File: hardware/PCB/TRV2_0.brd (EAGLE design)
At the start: 46 x 70 mm, 51 parts, among them IC1 TMP112, IC2 IC2, IC4 CNY70, IC5 ATMEGA8-AU, U1 DRV8850_RGY_24, X1 FC-12M

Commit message: ready for gerbers
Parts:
- added ML, MR: TPB1,27, testpad:B1,27
- moved J4 1.00 mm to (43.0, 21.0)
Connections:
- net ML: now also ML.TP
- net MR: now also MR.TP
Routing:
- net MR: track 32.3 -> 36.2 mm
- net ML: track 39.6 -> 41.9 mm
- net SPI_SCLK: track 43.1 -> 44.1 mm
- net SPI_MOSI: track 45.2 -> 46.2 mm
- net SPI_NNS: track 46.0 -> 47.0 mm
- net RFMIRQ: track 71.0 -> 72.0 mm
- net SPI_MISO: track 47.1 -> 48.1 mm
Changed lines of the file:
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@@
 <attribute name="NAME" x="14.7193" y="59.4741" size="0.8128" layer="25" rot="R180"/>
 </element>
-<element name="R5" library="resistor" package="R0603" value="4K7" x="10.7696" y="30.48" locked="yes" smashed="yes" rot="R90">
-<attribute name="NAME" x="-3.175" y="29.2354" size="0.8128" layer="25"/>
-</element>
+<element name="R5" library="resistor" package="R0603" value="4K7" x="10.7696" y="30.48" locked="yes" smashed="yes" rot="R90"/>
 <element name="R6" library="resistor" package="R0603" value="4K7" x="12.3952" y="30.48" locked="yes" smashed="yes" rot="R90">
 <attribute name="NAME" x="12.87145" y="32.22625" size="0.8128" layer="25" rot="R90"/>
@@
 <attribute name="VALUE" x="13.696009375" y="55.8038" size="1.27" layer="27" rot="R180"/>
 </element>
-<element name="J4" library="con-lstb" package="MA08-1" value="" x="42.005" y="20.955" rot="R90">
-<attribute name="MF" value="" x="42.005" y="20.955" size="1.778" layer="27" rot="R90" display="off"/>
-<attribute name="OC_NEWARK" value="unknown" x="42.005" y="20.955" size="1.778" layer="27" rot="R90" display="off"/>
-<attribute name="OC_FARNELL" value="unknown" x="42.005" y="20.955" size="1.778" layer="27" rot="R90" display="off"/>
-<attribute name="MPN" value="" x="42.005" y="20.955" size="1.778" layer="27" rot="R90" display="off"/>
+<element name="J4" library="con-lstb" package="MA08-1" value="" x="43.005" y="20.955" rot="R90">
+<attribute name="MF" value="" x="43.005" y="20.955" size="1.778" layer="27" rot="R90" display="off"/>
+<attribute name="OC_NEWARK" value="unknown" x="43.005" y="20.955" size="1.778" layer="27" rot="R90" display="off"/>
+<attribute name="OC_FARNELL" value="unknown" x="43.005" y="20.955" size="1.778" layer="27" rot="R90" display="off"/>
+<attribute name="MPN" value="" x="43.005" y="20.955" size="1.778" layer="27" rot="R90" display="off"/>
 </element>
 <element name="U1" library="drv8850" package="RGY_24" value="DRV8850_RGY_24" x="11.43" y="46.99" smashed="yes">
 <attribute name="VENDOR" value="Texas Instruments" x="11.43" y="46.99" size="1.778" layer="27" display="off"/>
 <attribute name="MANUFACTURER_PART_NUMBER" value="drv8850_rgy_24" x="11.43" y="46.99" size="1.778" layer="27" display="off"/>
-<attribute name="NAME" x="6.0198" y="48.5775" size="0.8128" layer="25" ratio="6" rot="SR0"/>
+<attribute name="NAME" x="6.387075" y="49.645740625" size="0.8128" layer="25" ratio="6" rot="SR0"/>
 </element>
 <element name="R3" library="resistor" package="R0603" value="24K" x="10.795" y="42.545" smashed="yes" rot="R180">
@@
 <element name="U$1" library="opto-trans-siemens" package="SFH_325-3/4" value="SFH_325-3/4" x="4.1473375" y="68.196" smashed="yes"/>
 <element name="U$2" library="led" package="KINGBRIGHTSIDELED" value="KINGBRIGHTSIDELED" x="13.17625" y="69.05625" smashed="yes" rot="MR0"/>
+<element name="ML" library="testpad" package="B1,27" value="TPB1,27" x="5.15581875" y="48.597771875" smashed="yes">
+<attribute name="TP_SIGNAL_NAME" value="" x="4.52081875" y="46.692771875" size="1" layer="37"/>
+<attribute name="NAME" x="4.049359375" y="48.0007" size="0.8128" layer="25" ratio="10" rot="R90"/>
+<attribute name="VALUE" x="4.52081875" y="47.835771875" size="0.0254" layer="27"/>
+</element>
+<element name="MR" library="testpad" package="B1,27" value="TPB1,27" x="5.1351375" y="46.475203125" smashed="yes">
+<attribute name="TP_SIGNAL_NAME" value="" x="4.5001375" y="44.570203125" size="1" layer="37"/>
+<attribute name="NAME" x="3.93528125" y="45.843521875" size="0.8128" layer="25" ratio="10" rot="R90"/>
+<attribute name="VALUE" x="4.5001375" y="45.713203125" size="0.0254" layer="27"/>
+</element>
 </elements>
 <signals>
@@
 <wire x1="21.9456" y1="17.8816" x2="22.073025" y2="17.996384375" width="0.2032" layer="1"/>
 <wire x1="21.9456" y1="17.272" x2="39.8272" y2="17.272" width="0.2032" layer="1"/>
-<wire x1="39.8272" y1="17.272" x2="42.005" y2="17.145" width="0.2032" layer="1"/>
+<wire x1="39.8272" y1="17.272" x2="43.005" y2="17.145" width="0.2032" layer="1"/>
 </signal>
 <signal name="MI">
@@
 <wire x1="13.60238125" y1="14.621740625" x2="15.340503125" y2="14.621740625" width="0.254" layer="16"/>
 <wire x1="21.336" y1="22.1488" x2="39.8272" y2="22.1488" width="0.2032" layer="1"/>
-<wire x1="39.8272" y1="22.1488" x2="42.005" y2="22.225" width="0.2032" layer="1"/>
+<wire x1="39.8272" y1="22.1488" x2="43.005" y2="22.225" width="0.2032" layer="1"/>
 <wire x1="21.336" y1="22.1488" x2="21.27013125" y2="21.97453125" width="0.2032" layer="1"/>
 <wire x1="15.4432" y1="14.6304" x2="15.337246875" y2="14.61893125" width="0.2032" layer="16"/>
@@
 <wire x1="22.7584" y1="24.5872" x2="39.8272" y2="24.5872" width="0.2032" layer="1"/>
 <wire x1="22.1488" y1="23.9776" x2="22.7584" y2="24.5872" width="0.2032" layer="1"/>
-<wire x1="39.8272" y1="24.5872" x2="42.005" y2="24.765" width="0.2032" layer="1"/>
+<wire x1="39.8272" y1="24.5872" x2="43.005" y2="24.765" width="0.2032" layer="1"/>
 <wire x1="22.1488" y1="23.9776" x2="22.098934375" y2="23.970465625" width="0.2032" layer="1"/>
 </signal>
@@
 <wire x1="22.352" y1="19.7104" x2="39.8272" y2="19.7104" width="0.2032" layer="1"/>
 <wire x1="22.1488" y1="19.9136" x2="22.352" y2="19.7104" width="0.2032" layer="1"/>
-<wire x1="39.8272" y1="19.7104" x2="42.005" y2="19.685" width="0.2032" layer="1"/>
+<wire x1="39.8272" y1="19.7104" x2="43.005" y2="19.685" width="0.2032" layer="1"/>
 <wire x1="22.1488" y1="19.9136" x2="22.034925" y2="20.030415625" width="0.2032" layer="1"/>
 </signal>
@@
 <wire x1="20.5232" y1="7.112" x2="21.5392" y2="8.128" width="0.2032" layer="1"/>
 <wire x1="20.5232" y1="6.096" x2="20.5232" y2="7.112" width="0.2032" layer="1"/>
-<wire x1="39.8272" y1="14.4272" x2="42.005" y2="14.605" width="0.2032" layer="1"/>
+<wire x1="39.8272" y1="14.4272" x2="43.005" y2="14.605" width="0.2032" layer="1"/>
 <wire x1="20.5232" y1="6.096" x2="20.4216" y2="6.096" width="0.2032" layer="1"/>
 </signal>
@@
 <via x="8.255" y="46.355" extent="1-16" drill="0.6"/>
 <wire x1="8.37" y1="46.24" x2="8.255" y2="46.355" width="0.2032" layer="1"/>
+<contactref element="ML" pad="TP"/>
+<wire x1="5.15581875" y1="48.597771875" x2="6.5913" y2="48.597771875" width="0.2032" layer="1"/>
+<wire x1="6.5913" y1="48.597771875" x2="6.5913" y2="47.752" width="0.2032" layer="1"/>
 </signal>
 <signal name="MR">
@@
 <wire x1="7.3025" y1="46.355" x2="7.3025" y2="47.24" width="0.2032" layer="1"/>
 <wire x1="7.3025" y1="47.24" x2="9.7026" y2="47.24" width="0.2032" layer="1"/>
+<contactref element="MR" pad="TP"/>
+<wire x1="5.1351375" y1="46.475203125" x2="5.132171875" y2="46.475203125" width="0.4064" layer="1"/>
+<wire x1="5.132171875" y1="46.475203125" x2="5.132171875" y2="44.0461125" width="0.2032" layer="1"/>
+<wire x1="5.132171875" y1="44.0461125" x2="6.1479875" y2="43.0694875" width="0.2032" layer="1"/>
 </signal>
 </signals>

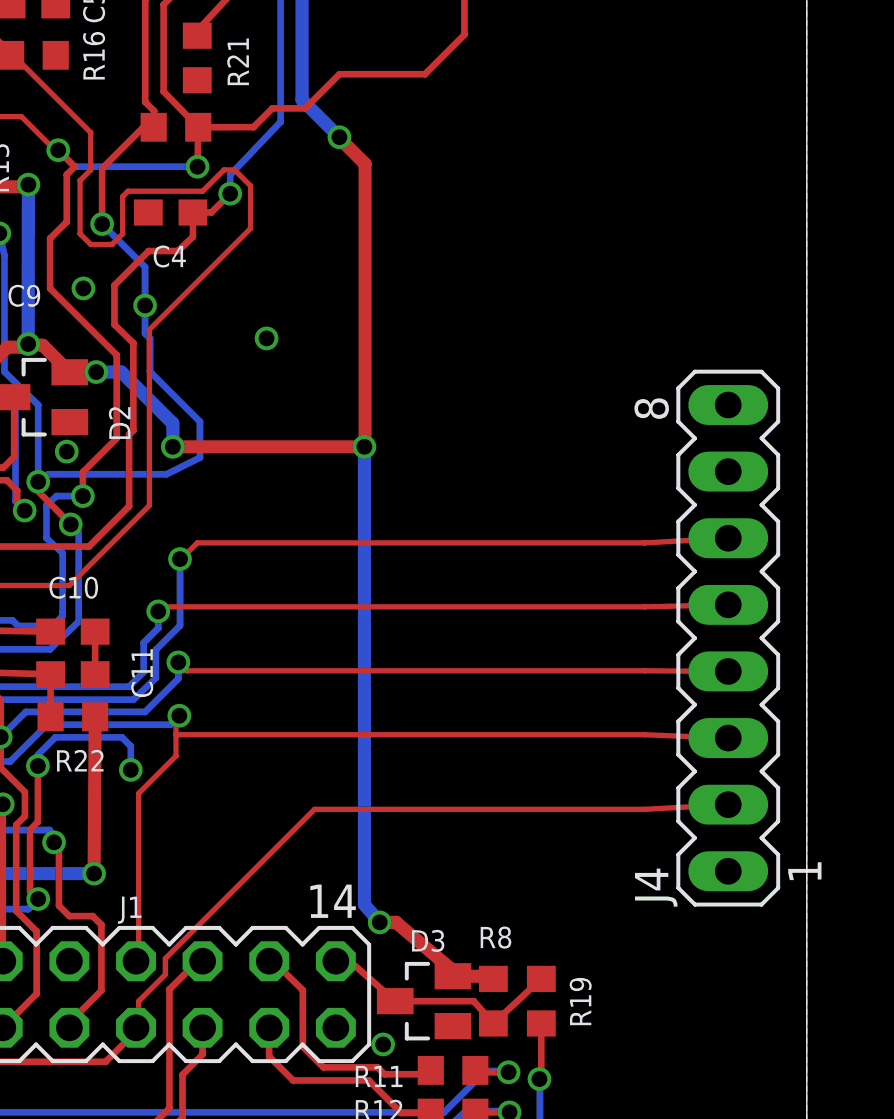
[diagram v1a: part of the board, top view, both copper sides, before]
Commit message: added power to radio module connector
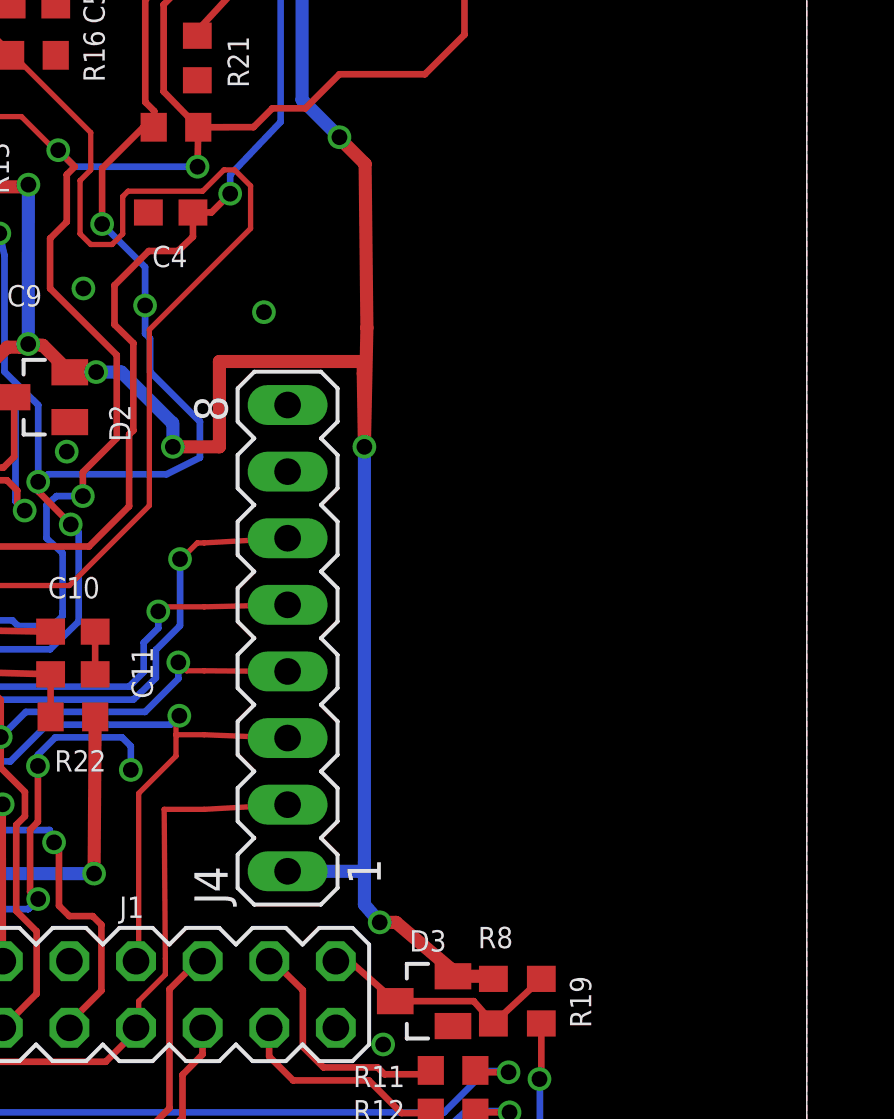
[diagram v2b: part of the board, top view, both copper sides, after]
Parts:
- moved J4 16.8 mm to (26.2, 21.0)
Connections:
- removed net RFVCC: J4.1
- net VCC: now also J4.1
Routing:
- net SPI_MOSI: track 46.2 -> 29.4 mm
- net SPI_NNS: track 47.0 -> 30.2 mm
- net SPI_SCLK: track 44.1 -> 27.3 mm
- net SPI_MISO: track 48.1 -> 31.3 mm
- net RFMIRQ: track 72.0 -> 58.6 mm
- net VCC: track 234.5 -> 244.2 mm
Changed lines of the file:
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@@
 <attribute name="VALUE" x="13.696009375" y="55.8038" size="1.27" layer="27" rot="R180"/>
 </element>
-<element name="J4" library="con-lstb" package="MA08-1" value="" x="43.005" y="20.955" rot="R90">
-<attribute name="MF" value="" x="43.005" y="20.955" size="1.778" layer="27" rot="R90" display="off"/>
-<attribute name="OC_NEWARK" value="unknown" x="43.005" y="20.955" size="1.778" layer="27" rot="R90" display="off"/>
-<attribute name="OC_FARNELL" value="unknown" x="43.005" y="20.955" size="1.778" layer="27" rot="R90" display="off"/>
-<attribute name="MPN" value="" x="43.005" y="20.955" size="1.778" layer="27" rot="R90" display="off"/>
+<element name="J4" library="con-lstb" package="MA08-1" value="" x="26.201871875" y="20.955" rot="R90">
+<attribute name="MF" value="" x="26.201871875" y="20.955" size="1.778" layer="27" rot="R90" display="off"/>
+<attribute name="OC_NEWARK" value="unknown" x="26.201871875" y="20.955" size="1.778" layer="27" rot="R90" display="off"/>
+<attribute name="OC_FARNELL" value="unknown" x="26.201871875" y="20.955" size="1.778" layer="27" rot="R90" display="off"/>
+<attribute name="MPN" value="" x="26.201871875" y="20.955" size="1.778" layer="27" rot="R90" display="off"/>
 </element>
 <element name="U1" library="drv8850" package="RGY_24" value="DRV8850_RGY_24" x="11.43" y="46.99" smashed="yes">
@@
 <via x="29.1301625" y="28.251125" extent="1-16" drill="0.6"/>
 <wire x1="29.713646875" y1="10.11754375" x2="29.1301625" y2="10.795" width="0.500125" layer="16"/>
-<wire x1="29.1301625" y1="10.795" x2="29.1301625" y2="28.251125" width="0.500125" layer="16"/>
+<wire x1="29.1301625" y1="10.795" x2="29.1301625" y2="12.407034375" width="0.500125" layer="16"/>
+<wire x1="29.1301625" y1="12.407034375" x2="29.1301625" y2="28.251125" width="0.500125" layer="16"/>
 <wire x1="21.82486875" y1="28.251125" x2="21.82486875" y2="29.16349375" width="0.500125" layer="16"/>
 <wire x1="19.86424375" y1="31.102021875" x2="18.902390625" y2="31.102021875" width="0.500125" layer="16"/>
 <wire x1="21.82486875" y1="29.16349375" x2="21.802771875" y2="29.16349375" width="0.254" layer="16"/>
 <wire x1="21.802771875" y1="29.16349375" x2="19.86424375" y2="31.102021875" width="0.500125" layer="16"/>
-<wire x1="21.82486875" y1="28.251125" x2="29.1301625" y2="28.251125" width="0.500125" layer="1"/>
+<wire x1="21.82486875" y1="28.251125" x2="23.60083125" y2="28.251125" width="0.500125" layer="1"/>
+<wire x1="23.60083125" y1="28.251125" x2="23.60083125" y2="31.504375" width="0.500125" layer="1"/>
+<wire x1="23.60083125" y1="31.504375" x2="29.085534375" y2="31.504375" width="0.500125" layer="1"/>
+<wire x1="29.085534375" y1="31.504375" x2="29.085534375" y2="31.0471875" width="0.500125" layer="1"/>
+<wire x1="29.085534375" y1="31.0471875" x2="29.1301625" y2="28.251125" width="0.500125" layer="1"/>
 <via x="26.882353125" y="56.752653125" extent="1-16" drill="0.6"/>
 <via x="28.1782625" y="40.057484375" extent="1-16" drill="0.6"/>
@@
 <wire x1="13.4112" y1="38.1644" x2="16.23338125" y2="38.1644" width="0.500125" layer="1"/>
 <wire x1="16.23338125" y1="38.1644" x2="16.317478125" y2="38.248496875" width="0.254" layer="1"/>
-<wire x1="29.15666875" y1="39.03951875" x2="29.15666875" y2="28.27763125" width="0.500125" layer="1"/>
+<wire x1="29.15666875" y1="39.03951875" x2="29.225921875" y2="32.789865625" width="0.500125" layer="1"/>
 <wire x1="28.1782625" y1="40.057484375" x2="28.1782625" y2="40.017925" width="0.254" layer="1"/>
 <wire x1="28.1782625" y1="40.017925" x2="29.15666875" y2="39.03951875" width="0.500125" layer="1"/>
-<wire x1="29.15666875" y1="28.27763125" x2="29.1301625" y2="28.251125" width="0.254" layer="1"/>
+<wire x1="29.225921875" y1="32.789865625" x2="29.1301625" y2="28.251125" width="0.500125" layer="1"/>
 <wire x1="26.882353125" y1="56.752653125" x2="26.928946875" y2="56.752653125" width="0.500125" layer="1"/>
 <wire x1="26.928946875" y1="56.752653125" x2="27.1666" y2="56.515" width="0.500125" layer="1"/>
@@
 <wire x1="26.8224" y1="56.896" x2="26.882353125" y2="56.752653125" width="0.2032" layer="1"/>
 <wire x1="13.1574" y1="47.24" x2="13.1574" y2="47.74" width="0.3048" layer="1"/>
+<contactref element="J4" pad="1"/>
+<wire x1="26.201871875" y1="12.065" x2="29.1301625" y2="12.065" width="0.500125" layer="16"/>
+<wire x1="29.1301625" y1="12.065" x2="29.1301625" y2="12.407034375" width="0.4064" layer="16"/>
 </signal>
 <signal name="GND">
@@
 <via x="3.81" y="32.385" extent="1-16" drill="0.6"/>
 <via x="10.795" y="38.735" extent="1-16" drill="0.6"/>
-<via x="25.4" y="32.385" extent="1-16" drill="0.6"/>
+<via x="25.299828125" y="33.386475" extent="1-16" drill="0.6"/>
 <via x="17.78" y="28.067" extent="1-16" drill="0.6"/>
 <wire x1="4.75120625" y1="38.2176" x2="6.2992" y2="38.2176" width="0.2032" layer="1"/>
@@
 <wire x1="20.5232" y1="8.7376" x2="20.4216" y2="8.636" width="0.2032" layer="1"/>
 <wire x1="21.9456" y1="17.8816" x2="22.073025" y2="17.996384375" width="0.2032" layer="1"/>
-<wire x1="21.9456" y1="17.272" x2="39.8272" y2="17.272" width="0.2032" layer="1"/>
-<wire x1="39.8272" y1="17.272" x2="43.005" y2="17.145" width="0.2032" layer="1"/>
+<wire x1="21.9456" y1="17.272" x2="23.024071875" y2="17.272" width="0.2032" layer="1"/>
+<wire x1="23.024071875" y1="17.272" x2="26.201871875" y2="17.145" width="0.2032" layer="1"/>
 </signal>
 <signal name="MI">
@@
 <wire x1="13.45586875" y1="14.475675" x2="13.60238125" y2="14.621740625" width="0.254" layer="16"/>
 <wire x1="13.60238125" y1="14.621740625" x2="15.340503125" y2="14.621740625" width="0.254" layer="16"/>
-<wire x1="21.336" y1="22.1488" x2="39.8272" y2="22.1488" width="0.2032" layer="1"/>
-<wire x1="39.8272" y1="22.1488" x2="43.005" y2="22.225" width="0.2032" layer="1"/>
+<wire x1="21.336" y1="22.1488" x2="23.024071875" y2="22.1488" width="0.2032" layer="1"/>
+<wire x1="23.024071875" y1="22.1488" x2="26.201871875" y2="22.225" width="0.2032" layer="1"/>
 <wire x1="21.336" y1="22.1488" x2="21.27013125" y2="21.97453125" width="0.2032" layer="1"/>
 <wire x1="15.4432" y1="14.6304" x2="15.337246875" y2="14.61893125" width="0.2032" layer="16"/>
@@
 <wire x1="22.098934375" y1="21.429446875" x2="22.098934375" y2="23.970465625" width="0.254" layer="16"/>
 <wire x1="14.2557125" y1="18.0657125" x2="14.757065625" y2="18.6092875" width="0.254" layer="16"/>
-<wire x1="22.7584" y1="24.5872" x2="39.8272" y2="24.5872" width="0.2032" layer="1"/>
+<wire x1="22.7584" y1="24.5872" x2="23.024071875" y2="24.5872" width="0.2032" layer="1"/>
 <wire x1="22.1488" y1="23.9776" x2="22.7584" y2="24.5872" width="0.2032" layer="1"/>
-<wire x1="39.8272" y1="24.5872" x2="43.005" y2="24.765" width="0.2032" layer="1"/>
+<wire x1="23.024071875" y1="24.5872" x2="26.201871875" y2="24.765" width="0.2032" layer="1"/>
 <wire x1="22.1488" y1="23.9776" x2="22.098934375" y2="23.970465625" width="0.2032" layer="1"/>
 </signal>
@@
 <wire x1="20.767975" y1="18.142434375" x2="16.220103125" y2="18.142434375" width="0.254" layer="16"/>
 <wire x1="16.220103125" y1="18.142434375" x2="15.261809375" y2="17.184584375" width="0.254" layer="16"/>
-<wire x1="22.352" y1="19.7104" x2="39.8272" y2="19.7104" width="0.2032" layer="1"/>
+<wire x1="22.352" y1="19.7104" x2="23.024071875" y2="19.7104" width="0.2032" layer="1"/>
 <wire x1="22.1488" y1="19.9136" x2="22.352" y2="19.7104" width="0.2032" layer="1"/>
-<wire x1="39.8272" y1="19.7104" x2="43.005" y2="19.685" width="0.2032" layer="1"/>
+<wire x1="23.024071875" y1="19.7104" x2="26.201871875" y2="19.685" width="0.2032" layer="1"/>
 <wire x1="22.1488" y1="19.9136" x2="22.034925" y2="20.030415625" width="0.2032" layer="1"/>
 </signal>
@@
 <wire x1="13.030671875" y1="3.962615625" x2="12.547384375" y2="3.962615625" width="0.254" layer="16"/>
 <wire x1="12.547384375" y1="3.962615625" x2="10.795" y2="5.715" width="0.254" layer="16"/>
-<wire x1="27.2288" y1="14.4272" x2="39.8272" y2="14.4272" width="0.2032" layer="1"/>
-<wire x1="21.5392" y1="8.7376" x2="27.2288" y2="14.4272" width="0.2032" layer="1"/>
+<wire x1="21.49479375" y1="14.4272" x2="23.024071875" y2="14.4272" width="0.2032" layer="1"/>
+<wire x1="21.5392" y1="8.7376" x2="21.49479375" y2="14.4272" width="0.2032" layer="1"/>
 <wire x1="21.5392" y1="8.128" x2="21.5392" y2="8.7376" width="0.2032" layer="1"/>
 <wire x1="20.5232" y1="7.112" x2="21.5392" y2="8.128" width="0.2032" layer="1"/>
 <wire x1="20.5232" y1="6.096" x2="20.5232" y2="7.112" width="0.2032" layer="1"/>
-<wire x1="39.8272" y1="14.4272" x2="43.005" y2="14.605" width="0.2032" layer="1"/>
+<wire x1="23.024071875" y1="14.4272" x2="26.201871875" y2="14.605" width="0.2032" layer="1"/>
 <wire x1="20.5232" y1="6.096" x2="20.4216" y2="6.096" width="0.2032" layer="1"/>
 </signal>
-<signal name="RFVCC">
-<contactref element="J4" pad="1"/>
-</signal>
 <signal name="BUTTON_MODE_L">
